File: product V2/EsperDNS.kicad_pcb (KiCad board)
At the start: 2 copper layers, 49 x 48 mm, 44 parts, among them J1 10118192-0001LF, J2 ARJM11A3, J3 Conn_02x05_Odd_Even, U1 AZ1117-3.3, U2 LAN8720A, U3 ESP32-WROOM-32D

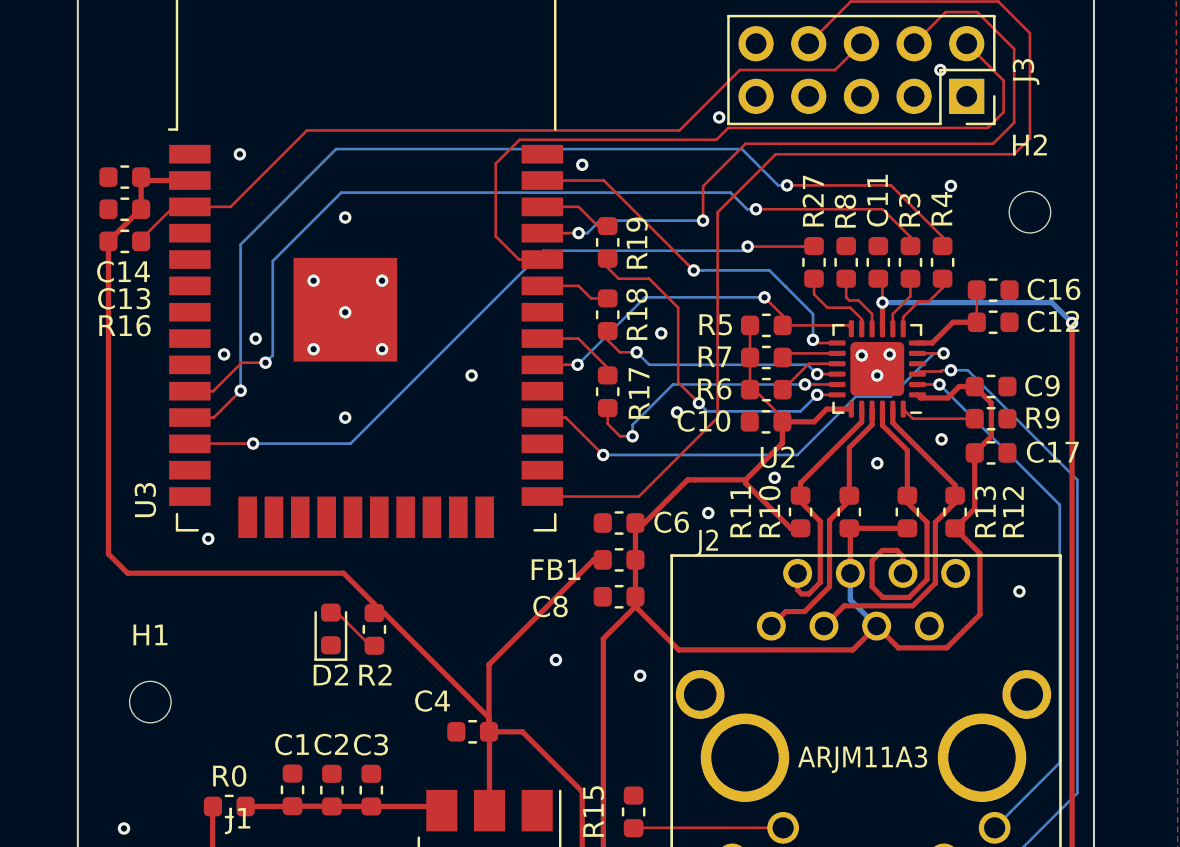
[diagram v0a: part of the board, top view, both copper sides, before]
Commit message: Editted traces to improve signal intregrity
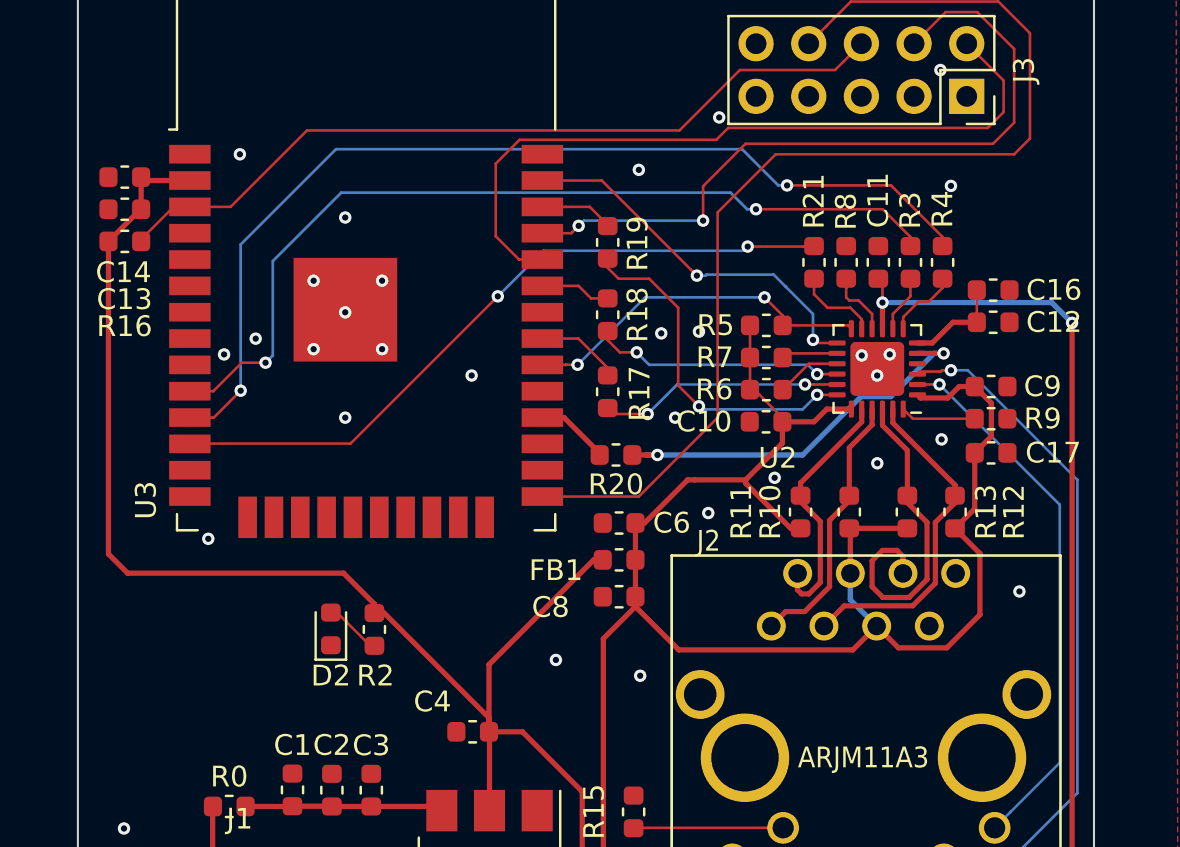
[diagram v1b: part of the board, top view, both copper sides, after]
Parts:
- removed H1, H2: MountingHole_Pad, MountingHole:MountingHole_2mm
- added R20: 100, Resistor_SMD:R_0603_1608Metric, F.Cu at (164.9, 90.7)
- renumbered R27 to R21
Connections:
- U2 pad 5: CLK50MHZ -> Net-(R20-Pad1)
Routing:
- net CLK50MHZ: track 23.4 -> 3.56 mm, vias 2 -> 0
- net Net-(R20-Pad1): track 0.00 -> 18.9 mm, vias 0 -> 2
- net TXD0: track 13.4 -> 11.8 mm
- net GND: vias 29 -> 30

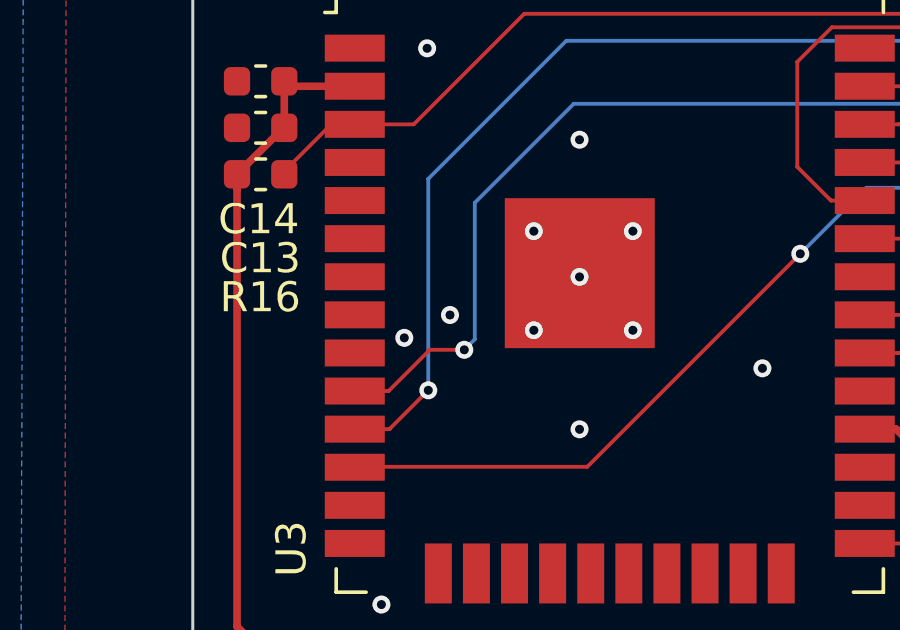
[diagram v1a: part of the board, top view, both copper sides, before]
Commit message: Started adding LEDs and pushbuttons to board
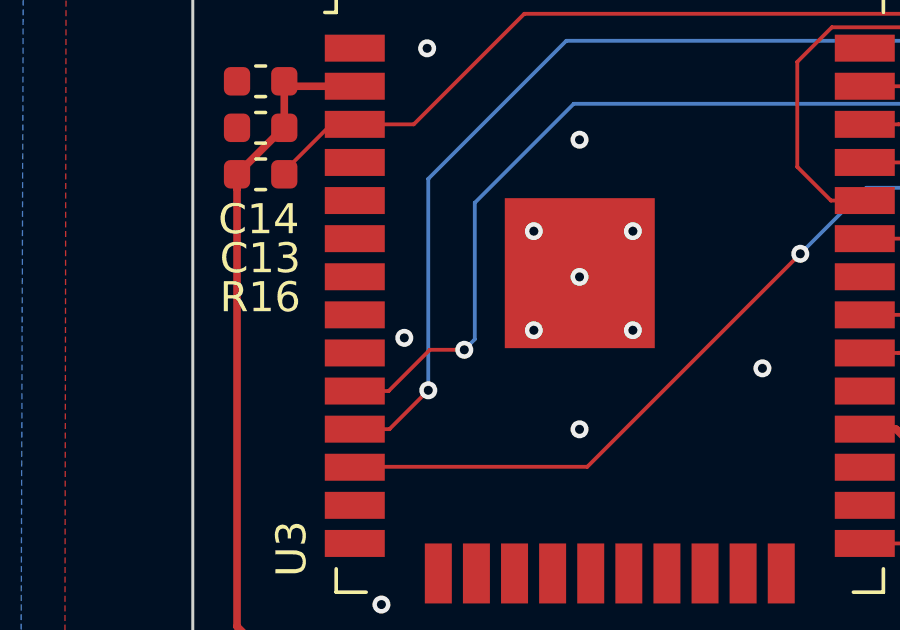
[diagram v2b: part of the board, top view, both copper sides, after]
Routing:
- net (no net): vias 1 -> 0
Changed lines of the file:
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@@
     (thickness 1.6)
     (drawings 6)
-    (tracks 405)
+    (tracks 404)
     (zones 0)
     (modules 43)
@@
   (gr_line (start 139 116) (end 139 68) (layer Edge.Cuts) (width 0.1))
   (gr_line (start 188 116) (end 139 116) (layer Edge.Cuts) (width 0.1))
-  (dimension 44.2 (width 0.12) (layer F.SilkS)
-    (gr_text "44.200 mm" (at 165.95 50.43) (layer F.SilkS)
-      (effects (font (size 1 1) (thickness 0.15)))
-    )
-    (feature1 (pts (xy 188.05 52.95) (xy 188.05 51.113579)))
-    (feature2 (pts (xy 143.85 52.95) (xy 143.85 51.113579)))
-    (crossbar (pts (xy 143.85 51.7) (xy 188.05 51.7)))
-    (arrow1a (pts (xy 188.05 51.7) (xy 186.923496 52.286421)))
-    (arrow1b (pts (xy 188.05 51.7) (xy 186.923496 51.113579)))
-    (arrow2a (pts (xy 143.85 51.7) (xy 144.976504 52.286421)))
-    (arrow2b (pts (xy 143.85 51.7) (xy 144.976504 51.113579)))
-  )
-  (dimension 47.55 (width 0.12) (layer F.SilkS)
-    (gr_text "47.550 mm" (at 121.830001 92.375 270) (layer F.SilkS)
-      (effects (font (size 1 1) (thickness 0.15)))
-    )
-    (feature1 (pts (xy 124.4 116.15) (xy 122.51358 116.15)))
-    (feature2 (pts (xy 124.4 68.6) (xy 122.51358 68.6)))
-    (crossbar (pts (xy 123.100001 68.6) (xy 123.100001 116.15)))
-    (arrow1a (pts (xy 123.100001 116.15) (xy 122.51358 115.023496)))
-    (arrow1b (pts (xy 123.100001 116.15) (xy 123.686422 115.023496)))
-    (arrow2a (pts (xy 123.100001 68.6) (xy 122.51358 69.726504)))
-    (arrow2b (pts (xy 123.100001 68.6) (xy 123.686422 69.726504)))
-  )
-  (via (at 147.574 85.09) (size 0.6) (drill 0.3) (layers F.Cu B.Cu) (net 0))
+  (dimension 49.050025 (width 0.12) (layer F.SilkS)
+    (gr_text "49.050 mm" (at 163.522329 50.505002 0.05840546347) (layer F.SilkS)
+      (effects (font (size 1 1) (thickness 0.15)))
+    )
+    (feature1 (pts (xy 188.05 53.1) (xy 188.048026 51.16358)))
+    (feature2 (pts (xy 139 53.15) (xy 138.998026 51.21358)))
+    (crossbar (pts (xy 138.998624 51.800001) (xy 188.048624 51.750001)))
+    (arrow1a (pts (xy 188.048624 51.750001) (xy 186.922719 52.33757)))
+    (arrow1b (pts (xy 188.048624 51.750001) (xy 186.921523 51.164729)))
+    (arrow2a (pts (xy 138.998624 51.800001) (xy 140.125725 52.385273)))
+    (arrow2b (pts (xy 138.998624 51.800001) (xy 140.124529 51.212432)))
+  )
+  (dimension 48.100234 (width 0.12) (layer F.SilkS)
+    (gr_text "48.100 mm" (at 121.905013 92.091986 89.82132351) (layer F.SilkS)
+      (effects (font (size 1 1) (thickness 0.15)))
+    )
+    (feature1 (pts (xy 124.4 116.15) (xy 122.513589 116.144117)))
+    (feature2 (pts (xy 124.55 68.05) (xy 122.663589 68.044117)))
+    (crossbar (pts (xy 123.250007 68.045946) (xy 123.100007 116.145946)))
+    (arrow1a (pts (xy 123.100007 116.145946) (xy 122.517102 115.017619)))
+    (arrow1b (pts (xy 123.100007 116.145946) (xy 123.689938 115.021276)))
+    (arrow2a (pts (xy 123.250007 68.045946) (xy 122.660076 69.170616)))
+    (arrow2b (pts (xy 123.250007 68.045946) (xy 123.832912 69.174273)))
+  )
   (via (at 151.892 83.82) (size 0.6) (drill 0.3) (layers F.Cu B.Cu) (net 1))
   (via (at 150.368 85.598) (size 0.6) (drill 0.3) (layers F.Cu B.Cu) (net 1))
@@
   (segment (start 176.8 84.6125) (end 176.8 84.15) (width 0.127) (layer F.Cu) (net 57))
   (segment (start 176.8 84.15) (end 176.25 83.6) (width 0.127) (layer F.Cu) (net 57))
-  (via (at 180.75 85.8) (size 0.6) (drill 0.3) (layers F.Cu B.Cu) (net 70))
-  (segment (start 180.75 85.8) (end 179.4875 85.8) (width 0.254) (layer F.Cu) (net 70))
   (segment (start 164.332 90.7) (end 164.332 90.7) (width 0.1778) (layer F.Cu) (net 58))
   (segment (start 162.445 88.895) (end 161.4 88.895) (width 0.254) (layer F.Cu) (net 58))
   (segment (start 164.1625 90.7) (end 164.1625 90.6125) (width 0.254) (layer F.Cu) (net 58))
   (segment (start 164.1625 90.6125) (end 162.445 88.895) (width 0.254) (layer F.Cu) (net 58))
-  (segment (start 173.95 90.7) (end 166.95 90.7) (width 0.254) (layer B.Cu) (net 70))
-  (segment (start 176.766 87.884) (end 173.95 90.7) (width 0.254) (layer B.Cu) (net 70))
-  (segment (start 178.199971 87.884) (end 176.766 87.884) (width 0.254) (layer B.Cu) (net 70))
-  (segment (start 180.75 85.8) (end 180.283971 85.8) (width 0.254) (layer B.Cu) (net 70))
-  (segment (start 180.283971 85.8) (end 178.199971 87.884) (width 0.254) (layer B.Cu) (net 70))
   (segment (start 179.15 83.05) (end 179.15 82.2) (width 0.127) (layer F.Cu) (net 59))
   (segment (start 178.3 84.6125) (end 178.3 83.9) (width 0.127) (layer F.Cu) (net 59))
@@
   (segment (start 164.55 79.6625) (end 164.55 79.6) (width 0.127) (layer F.Cu) (net 63))
   (segment (start 164.55 79.6) (end 163.685 78.735) (width 0.127) (layer F.Cu) (net 63))
+  (via (at 180.75 85.8) (size 0.6) (drill 0.3) (layers F.Cu B.Cu) (net 70))
+  (segment (start 180.75 85.8) (end 179.4875 85.8) (width 0.254) (layer F.Cu) (net 70))
+  (segment (start 173.95 90.7) (end 166.95 90.7) (width 0.254) (layer B.Cu) (net 70))
+  (segment (start 176.766 87.884) (end 173.95 90.7) (width 0.254) (layer B.Cu) (net 70))
+  (segment (start 178.199971 87.884) (end 176.766 87.884) (width 0.254) (layer B.Cu) (net 70))
+  (segment (start 180.75 85.8) (end 180.283971 85.8) (width 0.254) (layer B.Cu) (net 70))
+  (segment (start 180.283971 85.8) (end 178.199971 87.884) (width 0.254) (layer B.Cu) (net 70))
   (segment (start 166.95 90.7) (end 166.4 90.7) (width 0.254) (layer B.Cu) (net 70))
   (via (at 166.95 90.7) (size 0.6) (drill 0.3) (layers F.Cu B.Cu) (net 70))

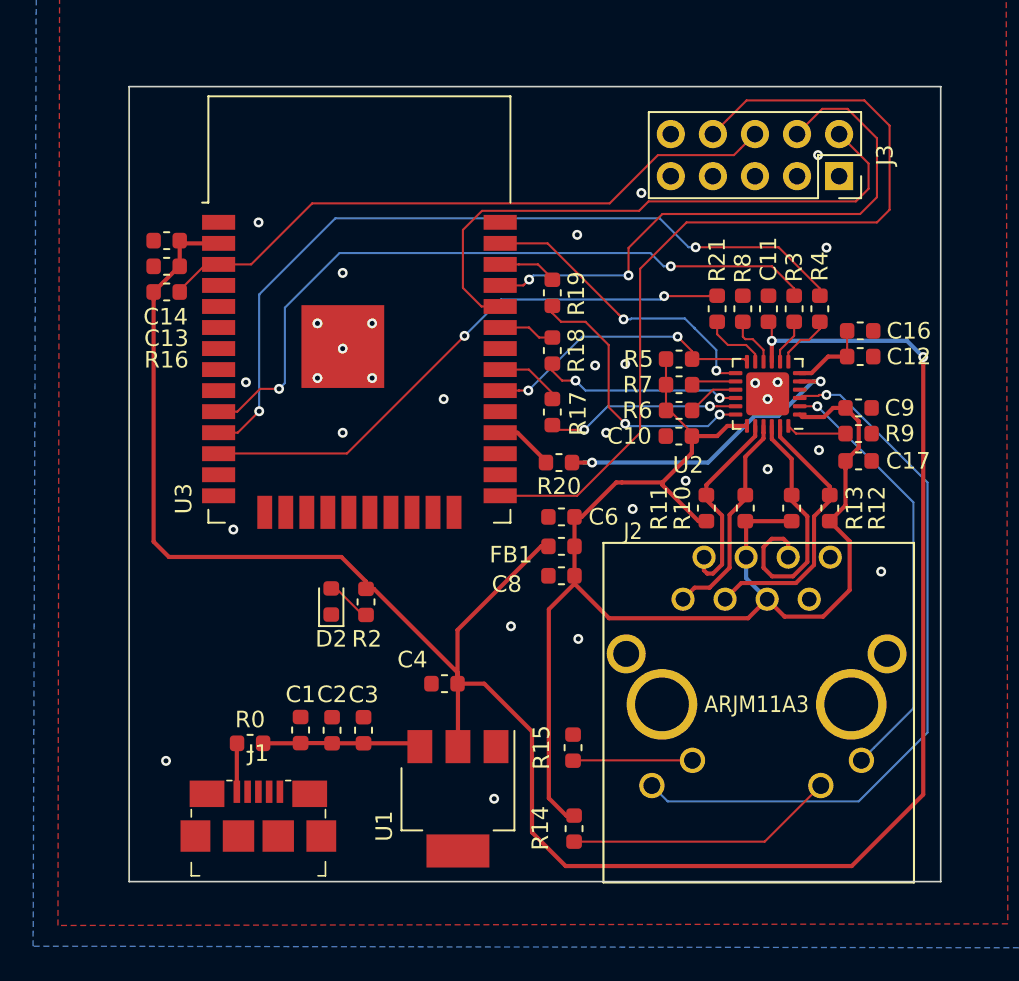
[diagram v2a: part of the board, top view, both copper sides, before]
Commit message: Added block button and RGB LED
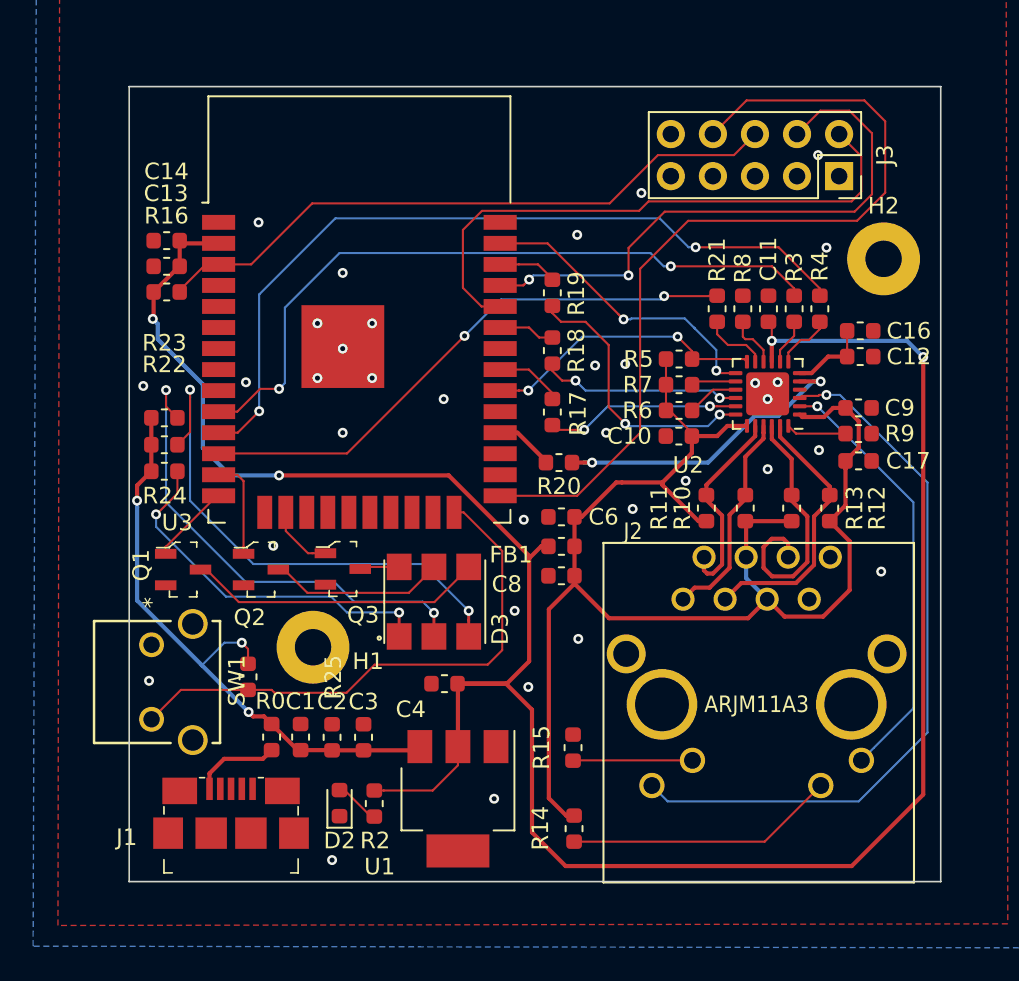
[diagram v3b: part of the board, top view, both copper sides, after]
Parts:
- added D3: CLP6C-FKB, My Footprints:CLP6C-FKB, F.Cu at (155.3, 101.2)
- added H1: MountingHole, MountingHole:MountingHole_2.2mm_M2_Pad, F.Cu at (150.1, 101.8)
- added H2: MountingHole, MountingHole:MountingHole_2.2mm_M2_Pad, F.Cu at (184.6, 78.4)
- added Q1: Q_NMOS_GSD, digikey-footprints:SOT-23-3, F.Cu at (142.3, 97.2)
- added Q2: Q_NMOS_GSD, digikey-footprints:SOT-23-3, F.Cu at (147.0, 97.2)
- added Q3: Q_NMOS_GSD, digikey-footprints:SOT-23-3, F.Cu at (151.9, 97.1)
- added R22: R, Resistor_SMD:R_0603_1608Metric, F.Cu at (141.1, 89.6)
- added R23: R, Resistor_SMD:R_0603_1608Metric, F.Cu at (141.1, 88.0)
- added R24: R, Resistor_SMD:R_0603_1608Metric, F.Cu at (141.1, 91.2)
- added R25: 10K, Resistor_SMD:R_0603_1608Metric, F.Cu at (146.2, 103.6)
- added SW1: 1-1825027-1, 1-1825027-1:1-1825027-1, F.Cu at (140.3, 101.7)
- moved D2 12.2 mm to (151.7, 111.3)
- moved R2 12.2 mm to (153.8, 111.3)
- moved J1 1.66 mm to (145.2, 113.1)
- moved R0 1.35 mm to (147.6, 107.3), turned to 90 degrees
- moved C1 0.43 mm to (149.3, 107.3)
- moved C2 0.42 mm to (151.2, 107.3)
- moved C3 0.42 mm to (153.2, 107.3)
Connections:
- U3 pad 13: Net-(U3-Pad13) -> Green
- U3 pad 14: Net-(U3-Pad14) -> Blue
- U3 pad 16: Net-(U3-Pad16) -> Red
- U3 pad 24: Net-(U3-Pad24) -> Block
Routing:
- net Block: track 0.00 -> 32.9 mm
- net Net-(D3-Pad3): track 0.00 -> 31.5 mm, vias 0 -> 2
- net Net-(D3-Pad2): track 0.00 -> 29.1 mm, vias 0 -> 2
- net VBUS: track 9.56 -> 36.7 mm, vias 0 -> 3
- net Net-(D3-Pad1): track 0.00 -> 22.2 mm, vias 0 -> 2
- net Net-(D3-Pad6): track 0.00 -> 17.9 mm
- net Net-(D3-Pad5): track 0.00 -> 10.7 mm
- net Green: track 0.00 -> 6.06 mm
- net +3V3: track 135.1 -> 140.0 mm, vias 2 -> 4
- net Blue: track 0.00 -> 4.90 mm
- net Red: track 0.00 -> 4.08 mm
- net Net-(D3-Pad4): track 0.00 -> 2.40 mm
- net Net-(J1-Pad1): track 2.93 -> 5.26 mm
- net BOOTMODE: track 53.7 -> 52.7 mm
- net RX: track 35.7 -> 35.1 mm
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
